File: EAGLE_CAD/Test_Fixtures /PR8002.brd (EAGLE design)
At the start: 122 x 89.3 mm, 58 parts, among them J1 M3_SCREW_POST

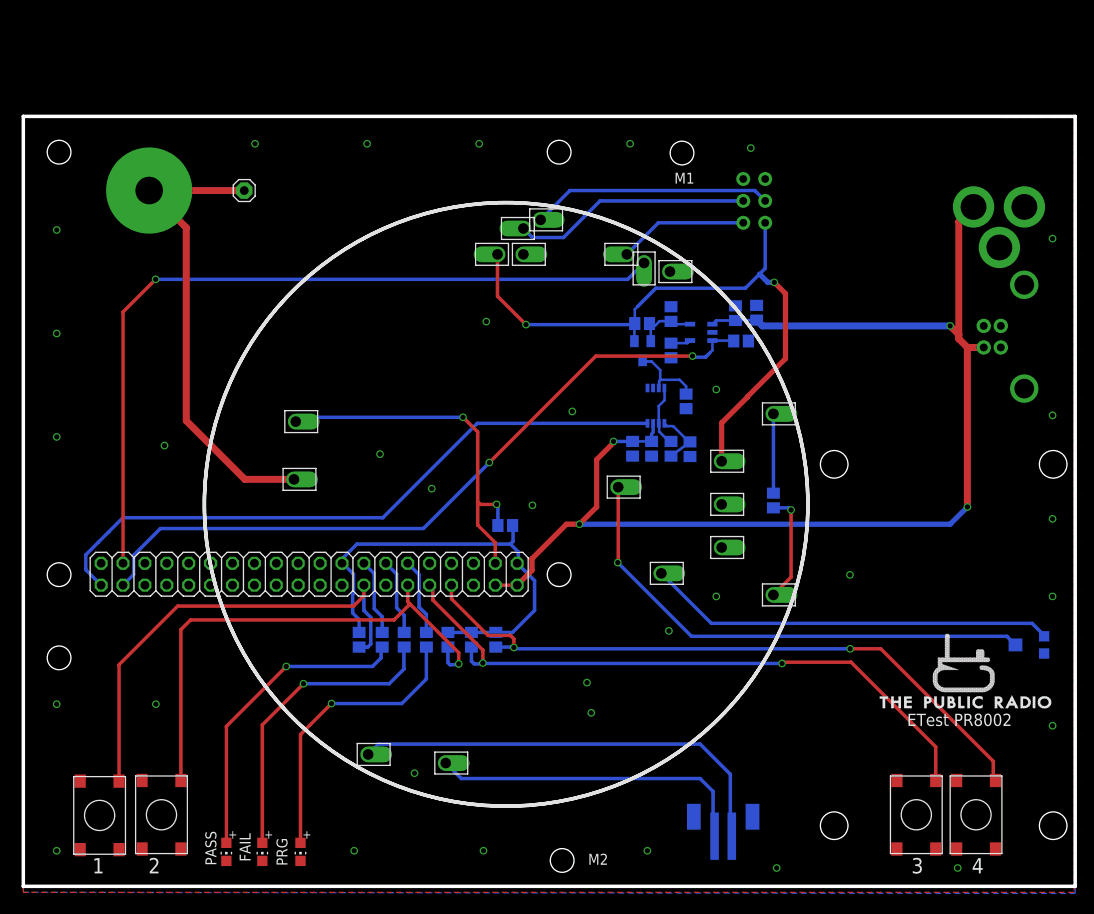
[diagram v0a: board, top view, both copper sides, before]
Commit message: PR8002 Updates
Moved TinyISP added more mounting holes, added additional SPK
connections.
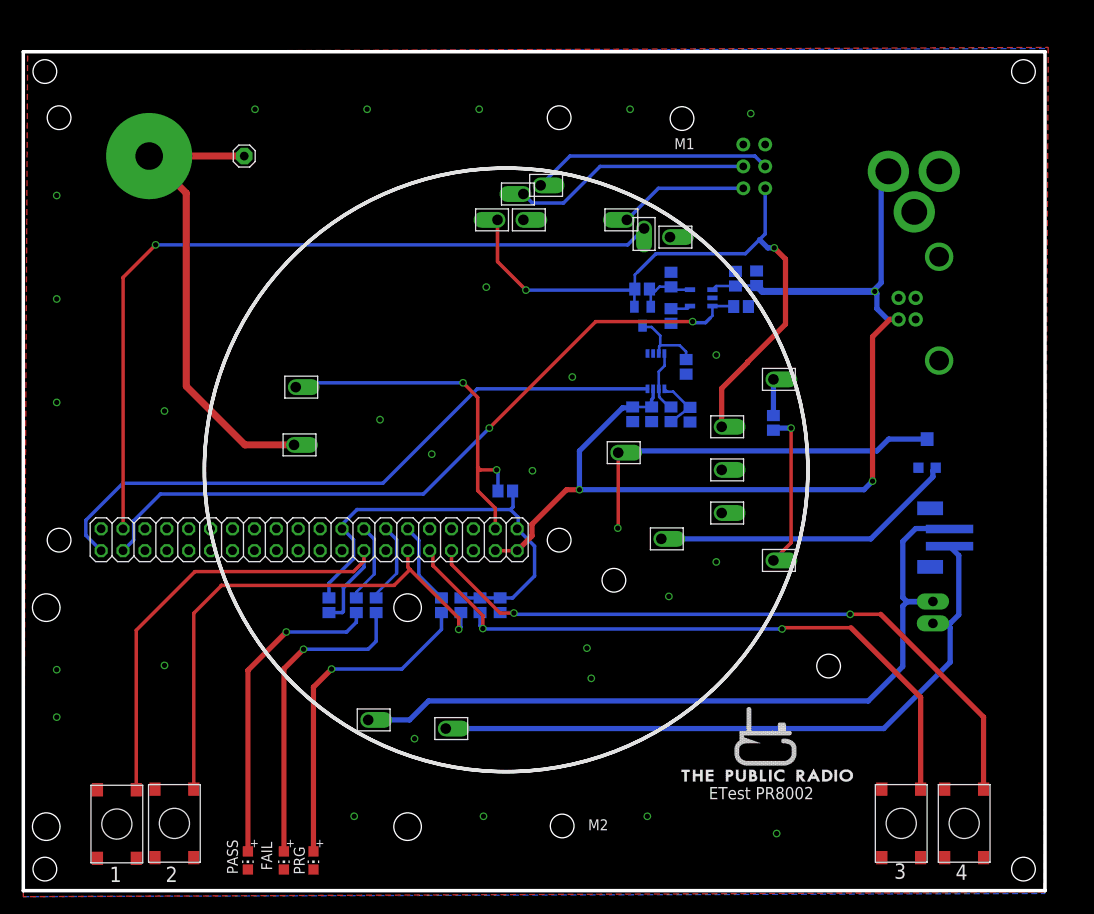
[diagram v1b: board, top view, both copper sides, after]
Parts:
- added JP2: M02PTH3, SparkFun-Connectors:1X02_LONGPADS
- moved U$25 83.0 mm to (24.8, 20.1), turned to 90 degrees
- moved CN1 39.6 mm to (105.2, 41.0), turned to 270 degrees
- moved VOL 25.3 mm to (105.3, 50.9), turned to 0 degrees
- moved U$1 24.5 mm to (86.6, 18.2)
- moved U$19 10.7 mm to (110.1, 83.3)
- moved JP1 10.4 mm to (104.0, 67.5)
- moved R14 9.00 mm to (87.5, 54.2)
- moved R13 5.32 mm to (36.0, 33.1)
- moved R1 5.15 mm to (41.4, 33.1)
- moved R3 5.00 mm to (39.1, 33.1)
- moved R9 4.37 mm to (49.0, 33.1)
- moved R12 4.27 mm to (51.2, 33.1)
- moved R11 4.12 mm to (53.5, 33.1)
- moved R10 4.03 mm to (55.8, 33.1)
- moved C3 4.00 mm to (75.6, 66.7)
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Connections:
- net SPK_OUT+: now also JP2.2
- net SPK_OUT-: now also JP2.1
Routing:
- net SPK_OUT-: track 38.6 -> 79.8 mm
- net SPK_OUT+: track 51.2 -> 91.6 mm
- net +5V: track 144.4 -> 124.7 mm, vias 4 -> 3
- net A_OUT: track 58.9 -> 45.3 mm
- net A_IN: track 47.5 -> 35.7 mm
- net SW_IN: track 12.9 -> 18.4 mm
- net N$2: track 33.5 -> 38.6 mm
- net SW_OUT: track 9.20 -> 4.20 mm
- net TAC4: track 55.1 -> 59.2 mm
- net TAC2: track 75.3 -> 78.7 mm
- net TAC1: track 77.3 -> 80.6 mm
- net TAC3: track 60.1 -> 61.5 mm
- net N$3: track 35.3 -> 36.5 mm
- net N$4: track 36.0 -> 37.0 mm
- net PROCESS: track 8.92 -> 9.64 mm
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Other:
- board size 122 x 89.3 mm -> 118.5 x 97.3 mm

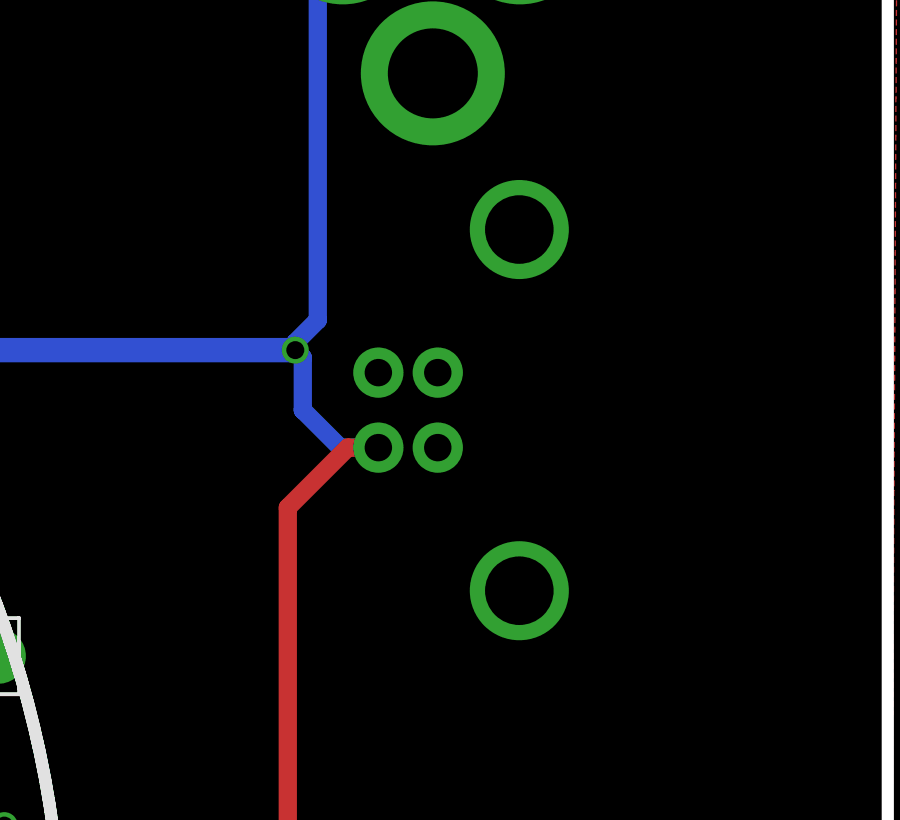
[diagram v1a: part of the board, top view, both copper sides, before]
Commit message: Updates PR8002
Removed USB jack for display
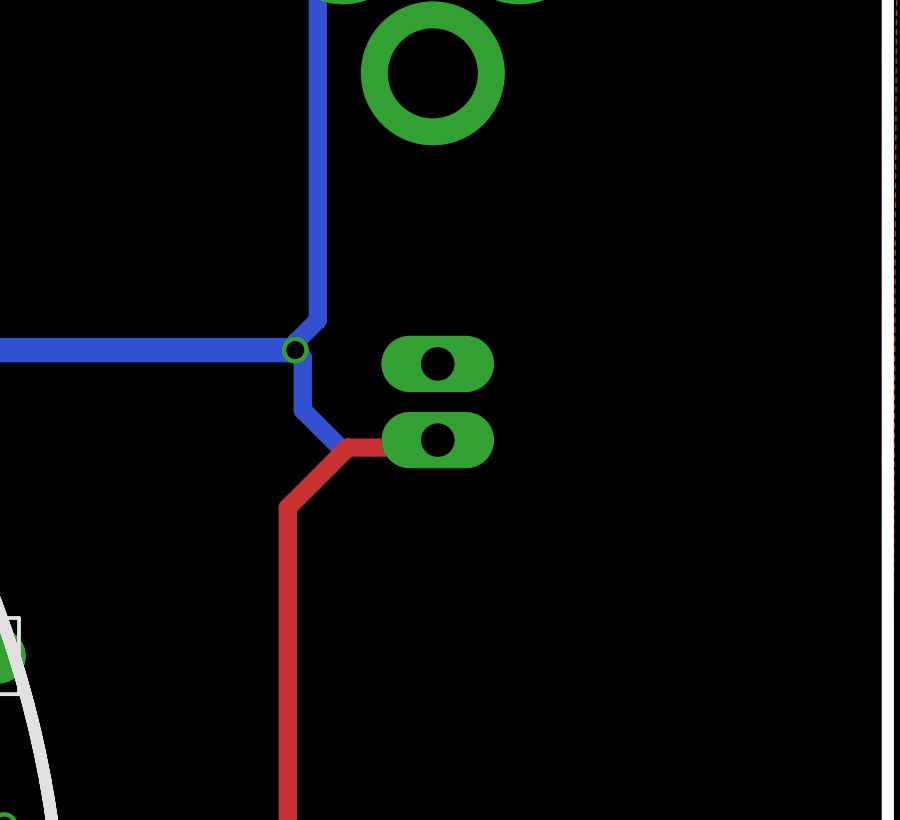
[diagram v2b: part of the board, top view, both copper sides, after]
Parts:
- removed JP1: USB-B, SparkFun-Connectors:USB-B-PTH
- added JP3: M02PTH3, SparkFun-Connectors:1X02_LONGPADS
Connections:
- net +5V: now also JP3.1; no longer JP1.VBUS
- net GND: now also JP3.2; no longer JP1.GND
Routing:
- net +5V: track 124.7 -> 125.5 mm
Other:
- board text added: "+ -"
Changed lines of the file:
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@@
 <hole x="116.5" y="2.5" drill="2.75"/>
 <hole x="93.9" y="26.05" drill="2.75"/>
+<text x="107.5" y="70.5" size="1.27" layer="22" font="vector" ratio="18" rot="MR270">+   -</text>
 </plain>
 <attributes>
@@
 <attribute name="VALUE" x="38.236" y="33.989" size="1.27" layer="28" rot="MR270"/>
 </element>
-<element name="JP1" library="SparkFun-Connectors" package="USB-B-PTH" value="USB-B" x="104" y="67.5" rot="MR0">
-<attribute name="PROD_ID" value="CONN-08278" x="104" y="67.5" size="1.778" layer="28" rot="MR0" display="off"/>
-</element>
 <element name="J1" library="PR_Parts_Library" package="M3_BOLT_HOLE" value="M3_SCREW_POST" x="15.1" y="85.2">
 <attribute name="MFG_PN" value="DNP" x="15.1" y="85.2" size="0.4064" layer="27" display="off"/>
@@
 </element>
 <element name="JP2" library="SparkFun-Connectors" package="1X02_LONGPADS" value="M02PTH3" x="106" y="31" rot="R90"/>
+<element name="JP3" library="SparkFun-Connectors" package="1X02_LONGPADS" value="M02PTH3" x="104" y="66.5" rot="R90"/>
 </elements>
 <signals>
@@
 <contactref element="U$20" pad="P$2"/>
 <contactref element="U$23" pad="P$2"/>
-<contactref element="JP1" pad="GND"/>
 <via x="59.55" y="48.7" extent="1-16" drill="0.6"/>
 <contactref element="GPIO" pad="6"/>
@@
 <via x="16.875" y="26.125" extent="1-16" drill="0.6"/>
 <via x="45.875" y="17.625" extent="1-16" drill="0.6"/>
+<contactref element="JP3" pad="2"/>
 </signal>
 <signal name="A_OUT">
@@
 <wire x1="73.375" y1="56.1" x2="73.375" y2="56.975" width="0.4064" layer="16"/>
 <wire x1="73.55" y1="57.15" x2="73.55" y2="58.2" width="0.4064" layer="16"/>
-<contactref element="JP1" pad="VBUS"/>
 <wire x1="73.375" y1="56.975" x2="73.55" y2="57.15" width="0.3048" layer="16"/>
 <wire x1="73.375" y1="56.1" x2="71.175" y2="56.1" width="0.3048" layer="16"/>
@@
 <wire x1="63.5" y1="46.5" x2="65" y2="46.5" width="0.6096" layer="1"/>
 <via x="65" y="46.5" extent="1-16" drill="0.6" diameter="0.6096"/>
-<wire x1="102.0188" y1="66.25" x2="100.75" y2="66.25" width="0.6096" layer="16"/>
 <wire x1="100.75" y1="66.25" x2="99.5" y2="67.5" width="0.6096" layer="16"/>
 <wire x1="99.5" y1="67.5" x2="99.5" y2="69.25" width="0.6096" layer="16"/>
@@
 <wire x1="99" y1="47.5" x2="99" y2="64.25" width="0.6096" layer="1"/>
 <wire x1="99" y1="64.25" x2="101" y2="66.25" width="0.6096" layer="1"/>
-<wire x1="101" y1="66.25" x2="102.0188" y2="66.25" width="0.6096" layer="1"/>
 <wire x1="65" y1="46.5" x2="65" y2="51" width="0.6096" layer="16"/>
 <wire x1="65" y1="51" x2="70" y2="56" width="0.6096" layer="16"/>
 <wire x1="70" y1="56" x2="71.075" y2="56" width="0.6096" layer="16"/>
 <wire x1="71.075" y1="56" x2="71.175" y2="56.1" width="0.6096" layer="16"/>
+<contactref element="JP3" pad="1"/>
+<wire x1="101" y1="66.25" x2="103.75" y2="66.25" width="0.6096" layer="1"/>
+<wire x1="103.75" y1="66.25" x2="104" y2="66.5" width="0.6096" layer="1"/>
+<wire x1="101" y1="66.25" x2="100.75" y2="66.25" width="0" layer="19" extent="1-16"/>
 </signal>
 <signal name="GPIO4">

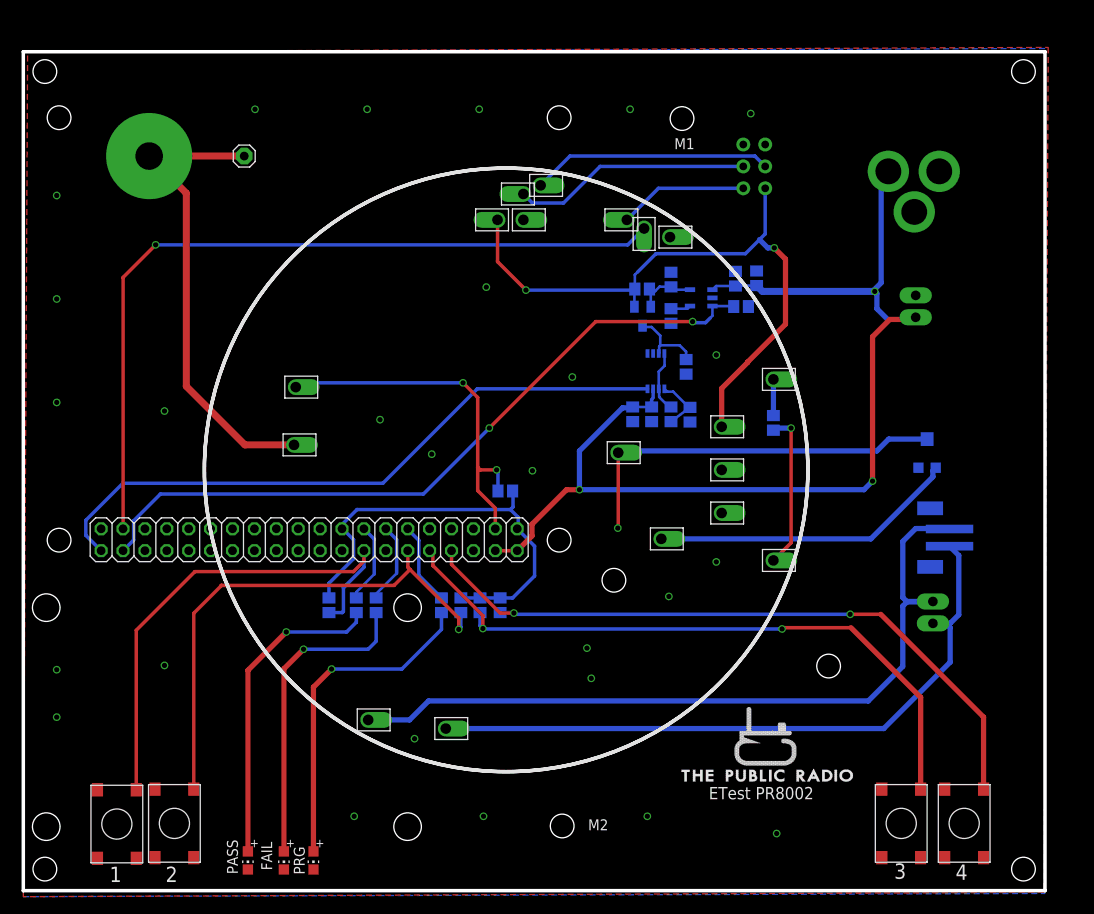
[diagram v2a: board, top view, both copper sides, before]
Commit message: PR8002 Updates
 Moved RPI slightly, added room around mounting holes.
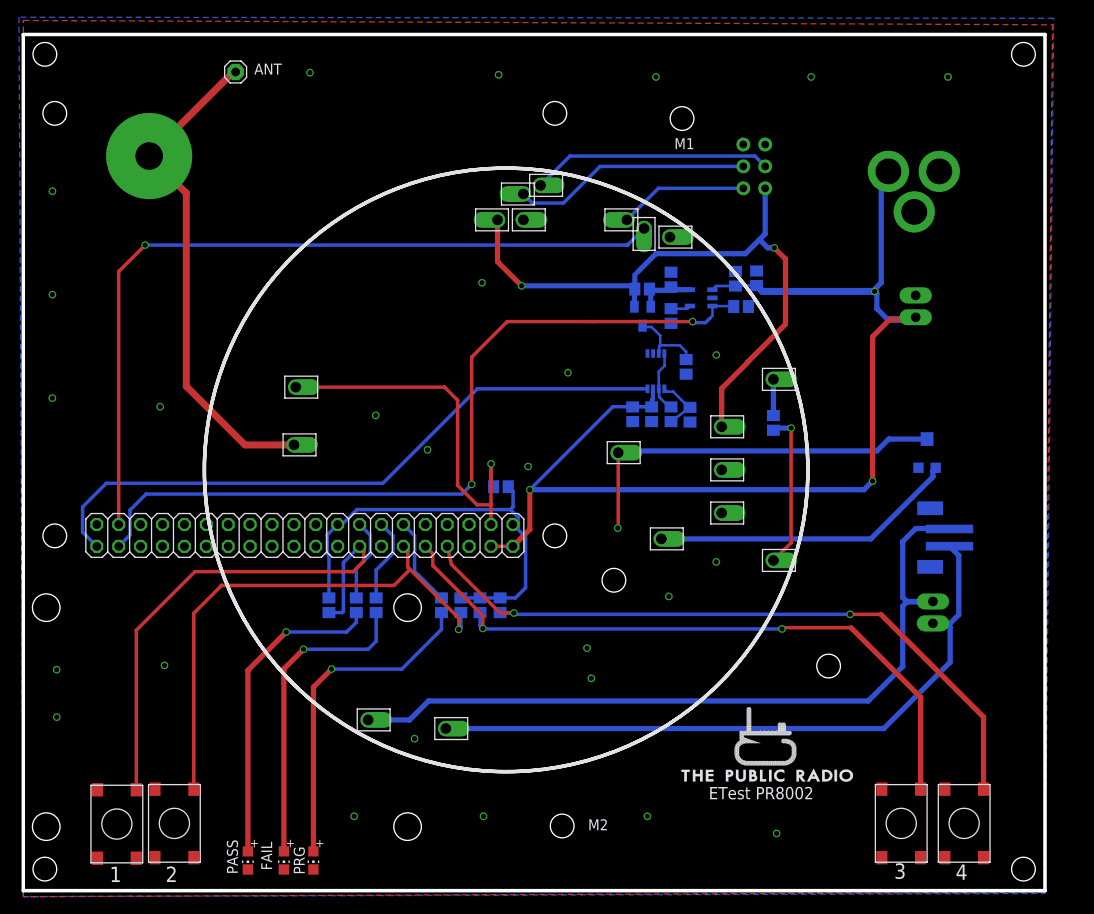
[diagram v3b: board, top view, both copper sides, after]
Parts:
- moved ANT 9.80 mm to (25.1, 95.0)
- moved GPIO 0.71 mm to (33.2, 41.2)
- moved R2 0.71 mm to (55.9, 46.9)
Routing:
- net +5V: track 125.5 -> 139.0 mm
- net REG_ENABLE: track 84.7 -> 94.0 mm
- net ANT: track 54.8 -> 57.9 mm
- net TAC4: track 59.2 -> 60.9 mm
- net PROCESS: track 9.64 -> 11.1 mm
- net DEV_PRES: track 42.9 -> 43.9 mm, vias 2 -> 1
- net COMPARATOR: track 75.7 -> 76.5 mm
- net TAC3: track 61.5 -> 62.2 mm
- net TAC2: track 78.7 -> 79.4 mm
- net TAC1: track 80.6 -> 81.2 mm
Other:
- board size 118.5 x 97.3 mm -> 118.5 x 99.3 mm

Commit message: Updates to PR8002
Updates to PR8002
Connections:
- net SPK_OUT-: no longer JP2.1
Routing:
- net SPK_OUT-: track 79.8 -> 76.3 mm
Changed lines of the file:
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@@
 <wire x1="100.3" y1="18.8" x2="108" y2="26.5" width="0.6096" layer="16"/>
 <wire x1="108" y1="39.875" x2="107.925" y2="39.95" width="0.6096" layer="16"/>
-<contactref element="JP2" pad="1"/>
 <wire x1="108" y1="26.5" x2="108" y2="30.5" width="0.6096" layer="16"/>
 <wire x1="108" y1="30.5" x2="107.5" y2="31" width="0.6096" layer="16"/>
-<wire x1="107.5" y1="31" x2="106" y2="31" width="0.6096" layer="16"/>
-<wire x1="106" y1="31" x2="108" y2="31" width="0.6096" layer="16"/>
 <wire x1="108" y1="31" x2="109" y2="32" width="0.6096" layer="16"/>
 <wire x1="109" y1="32" x2="109" y2="38.875" width="0.6096" layer="16"/>
 <wire x1="109" y1="38.875" x2="107.925" y2="39.95" width="0.6096" layer="16"/>
+<wire x1="108" y1="30.5" x2="108" y2="31" width="0" layer="19" extent="16-16"/>
 </signal>
 <signal name="MISO">
